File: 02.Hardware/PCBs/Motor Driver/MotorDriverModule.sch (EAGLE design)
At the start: 45 parts, among them Q1 DMC3021LSD-13, Q2 DMC3021LSD-13, Q3 DMC3021LSD-13, U1 FAN3268TMX, U2 FAN3268TMX, U3 FAN3268TMX, U4 MCP6001T-I_LT

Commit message: Minor modifications
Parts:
- added C9: (no value), rcl:C-EUC0805
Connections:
- net GND: now also C9.2
- net VCC: now also C9.1
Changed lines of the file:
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@@
 <part name="GND25" library="SparkFun-PowerSymbols" library_urn="urn:adsk.eagle:library:530" deviceset="GND" device=""/>
 <part name="J5" library="SparkFun-Connectors" library_urn="urn:adsk.eagle:library:513" deviceset="CONN_10" device="&quot;" package3d_urn="urn:adsk.eagle:package:38157/1"/>
+<part name="C9" library="rcl" library_urn="urn:adsk.eagle:library:334" deviceset="C-EU" device="C0805" package3d_urn="urn:adsk.eagle:package:23617/2"/>
+<part name="SUPPLY7" library="SparkFun-PowerSymbols" library_urn="urn:adsk.eagle:library:530" deviceset="VCC" device=""/>
+<part name="GND24" library="SparkFun-PowerSymbols" library_urn="urn:adsk.eagle:library:530" deviceset="GND" device=""/>
 </parts>
 <sheets>
@@
 <attribute name="NAME" x="330.2" y="78.232" size="1.778" layer="95" font="vector" rot="R180"/>
 </instance>
+<instance part="C9" gate="G$1" x="274.32" y="129.54" smashed="yes">
+<attribute name="NAME" x="275.844" y="129.921" size="1.778" layer="95"/>
+<attribute name="VALUE" x="275.844" y="124.841" size="1.778" layer="96"/>
+</instance>
+<instance part="SUPPLY7" gate="G$1" x="274.32" y="132.08" smashed="yes">
+<attribute name="VALUE" x="274.32" y="134.874" size="1.778" layer="96" align="bottom-center"/>
+</instance>
+<instance part="GND24" gate="1" x="274.32" y="121.92" smashed="yes">
+<attribute name="VALUE" x="274.32" y="121.666" size="1.778" layer="96" align="top-center"/>
+</instance>
 </instances>
 <busses>
@@
 <wire x1="320.04" y1="35.56" x2="302.26" y2="35.56" width="0.1524" layer="91"/>
 <label x="304.8" y="35.56" size="1.778" layer="95"/>
+</segment>
+<segment>
+<pinref part="C9" gate="G$1" pin="2"/>
+<pinref part="GND24" gate="1" pin="GND"/>
 </segment>
 </net>
@@
 <label x="304.8" y="33.02" size="1.778" layer="95"/>
 </segment>
-</net>
+<segment>
+<pinref part="C9" gate="G$1" pin="1"/>
+<pinref part="SUPPLY7" gate="G$1" pin="VCC"/>
+</segment>
+</net>

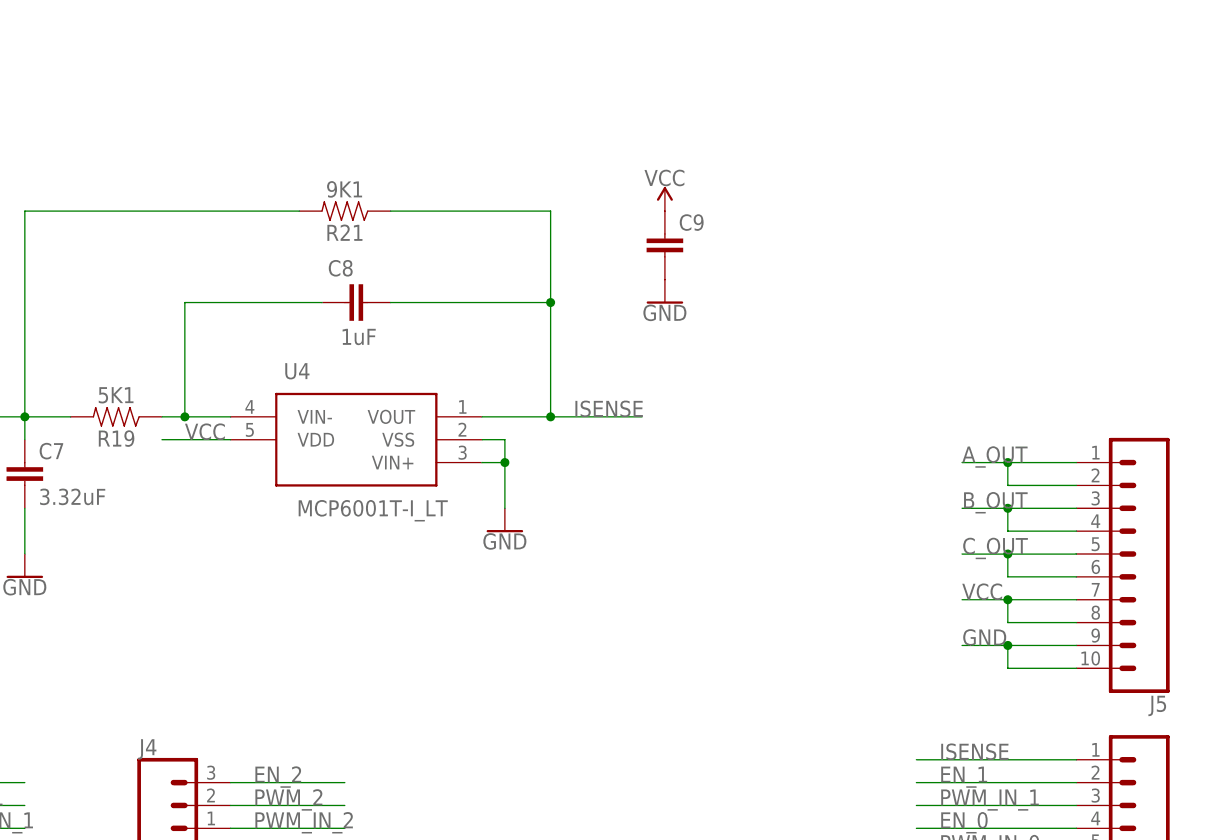
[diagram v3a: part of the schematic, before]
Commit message: añadido 3v3 a driver de motor
Para que el AO filtro de ISENSE se alimente a 3v3
Se actualiza GERBER para PCBWAY
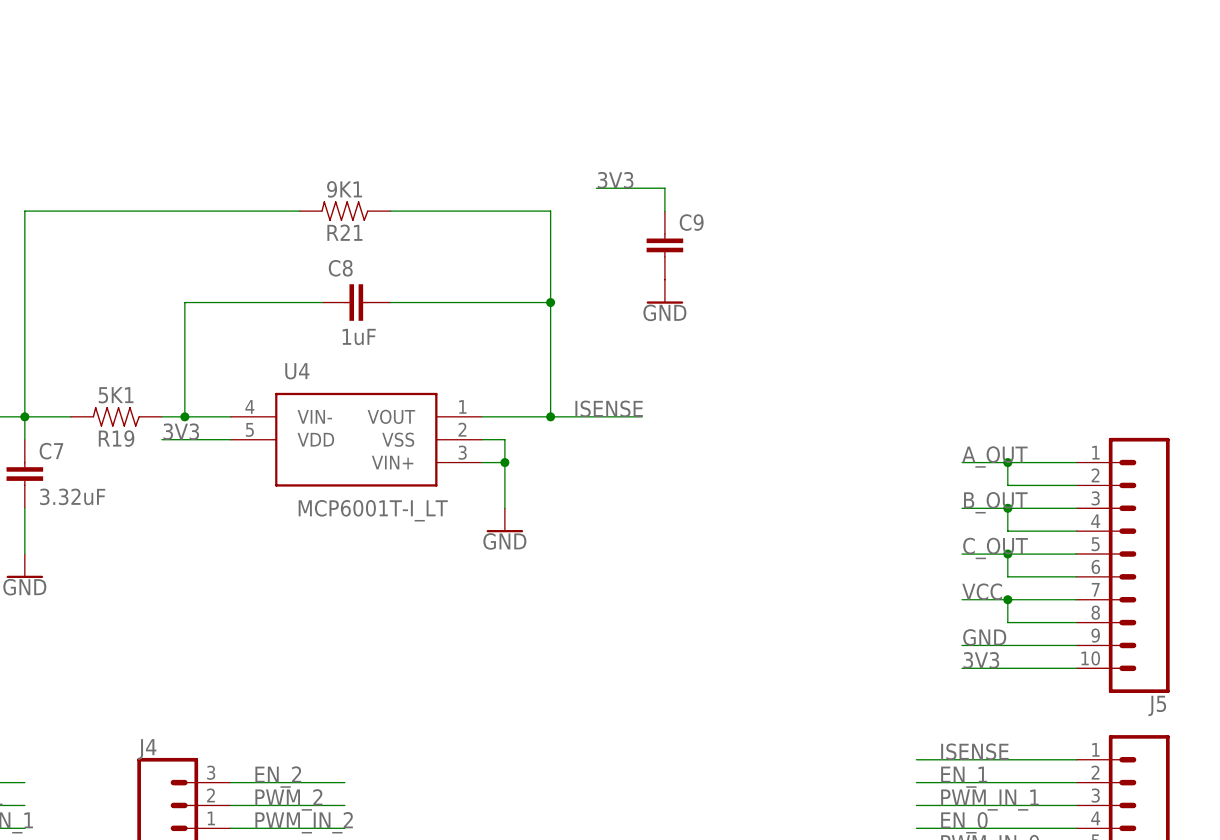
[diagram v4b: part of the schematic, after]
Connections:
- new net 3V3: C9.1, J5.10, U4.VDD
- net GND: no longer J5.10
- net VCC: no longer C9.1, U4.VDD
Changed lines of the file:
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@@
 <part name="J5" library="SparkFun-Connectors" library_urn="urn:adsk.eagle:library:513" deviceset="CONN_10" device="&quot;" package3d_urn="urn:adsk.eagle:package:38157/1"/>
 <part name="C9" library="rcl" library_urn="urn:adsk.eagle:library:334" deviceset="C-EU" device="C0805" package3d_urn="urn:adsk.eagle:package:23617/2"/>
-<part name="SUPPLY7" library="SparkFun-PowerSymbols" library_urn="urn:adsk.eagle:library:530" deviceset="VCC" device=""/>
 <part name="GND24" library="SparkFun-PowerSymbols" library_urn="urn:adsk.eagle:library:530" deviceset="GND" device=""/>
 </parts>
@@
 <attribute name="VALUE" x="275.844" y="124.841" size="1.778" layer="96"/>
 </instance>
-<instance part="SUPPLY7" gate="G$1" x="274.32" y="132.08" smashed="yes">
-<attribute name="VALUE" x="274.32" y="134.874" size="1.778" layer="96" align="bottom-center"/>
-</instance>
 <instance part="GND24" gate="1" x="274.32" y="121.92" smashed="yes">
 <attribute name="VALUE" x="274.32" y="121.666" size="1.778" layer="96" align="top-center"/>
@@
 <segment>
 <pinref part="J5" gate="G$1" pin="9"/>
-<wire x1="320.04" y1="83.82" x2="312.42" y2="83.82" width="0.1524" layer="91"/>
-<pinref part="J5" gate="G$1" pin="10"/>
-<wire x1="312.42" y1="83.82" x2="307.34" y2="83.82" width="0.1524" layer="91"/>
-<wire x1="320.04" y1="81.28" x2="312.42" y2="81.28" width="0.1524" layer="91"/>
-<wire x1="312.42" y1="81.28" x2="312.42" y2="83.82" width="0.1524" layer="91"/>
-<junction x="312.42" y="83.82"/>
+<wire x1="320.04" y1="83.82" x2="307.34" y2="83.82" width="0.1524" layer="91"/>
 <label x="307.34" y="83.82" size="1.778" layer="95"/>
 </segment>
@@
 </segment>
 <segment>
-<pinref part="U4" gate="G$1" pin="VDD"/>
-<wire x1="226.06" y1="106.68" x2="218.44" y2="106.68" width="0.1524" layer="91"/>
-<label x="220.98" y="106.68" size="1.778" layer="95"/>
-</segment>
-<segment>
 <pinref part="J5" gate="G$1" pin="7"/>
 <wire x1="320.04" y1="88.9" x2="312.42" y2="88.9" width="0.1524" layer="91"/>
@@
 <wire x1="320.04" y1="33.02" x2="302.26" y2="33.02" width="0.1524" layer="91"/>
 <label x="304.8" y="33.02" size="1.778" layer="95"/>
-</segment>
-<segment>
-<pinref part="C9" gate="G$1" pin="1"/>
-<pinref part="SUPPLY7" gate="G$1" pin="VCC"/>
 </segment>
 </net>
@@
 </segment>
 </net>
+<net name="3V3" class="0">
+<segment>
+<pinref part="J5" gate="G$1" pin="10"/>
+<wire x1="320.04" y1="81.28" x2="307.34" y2="81.28" width="0.1524" layer="91"/>
+<label x="307.34" y="81.28" size="1.778" layer="95"/>
+</segment>
+<segment>
+<pinref part="U4" gate="G$1" pin="VDD"/>
+<wire x1="226.06" y1="106.68" x2="218.44" y2="106.68" width="0.1524" layer="91"/>
+<label x="218.44" y="106.68" size="1.778" layer="95"/>
+</segment>
+<segment>
+<pinref part="C9" gate="G$1" pin="1"/>
+<wire x1="274.32" y1="132.08" x2="274.32" y2="134.62" width="0.1524" layer="91"/>
+<wire x1="274.32" y1="134.62" x2="266.7" y2="134.62" width="0.1524" layer="91"/>
+<label x="266.7" y="134.62" size="1.778" layer="95"/>
+</segment>
+</net>

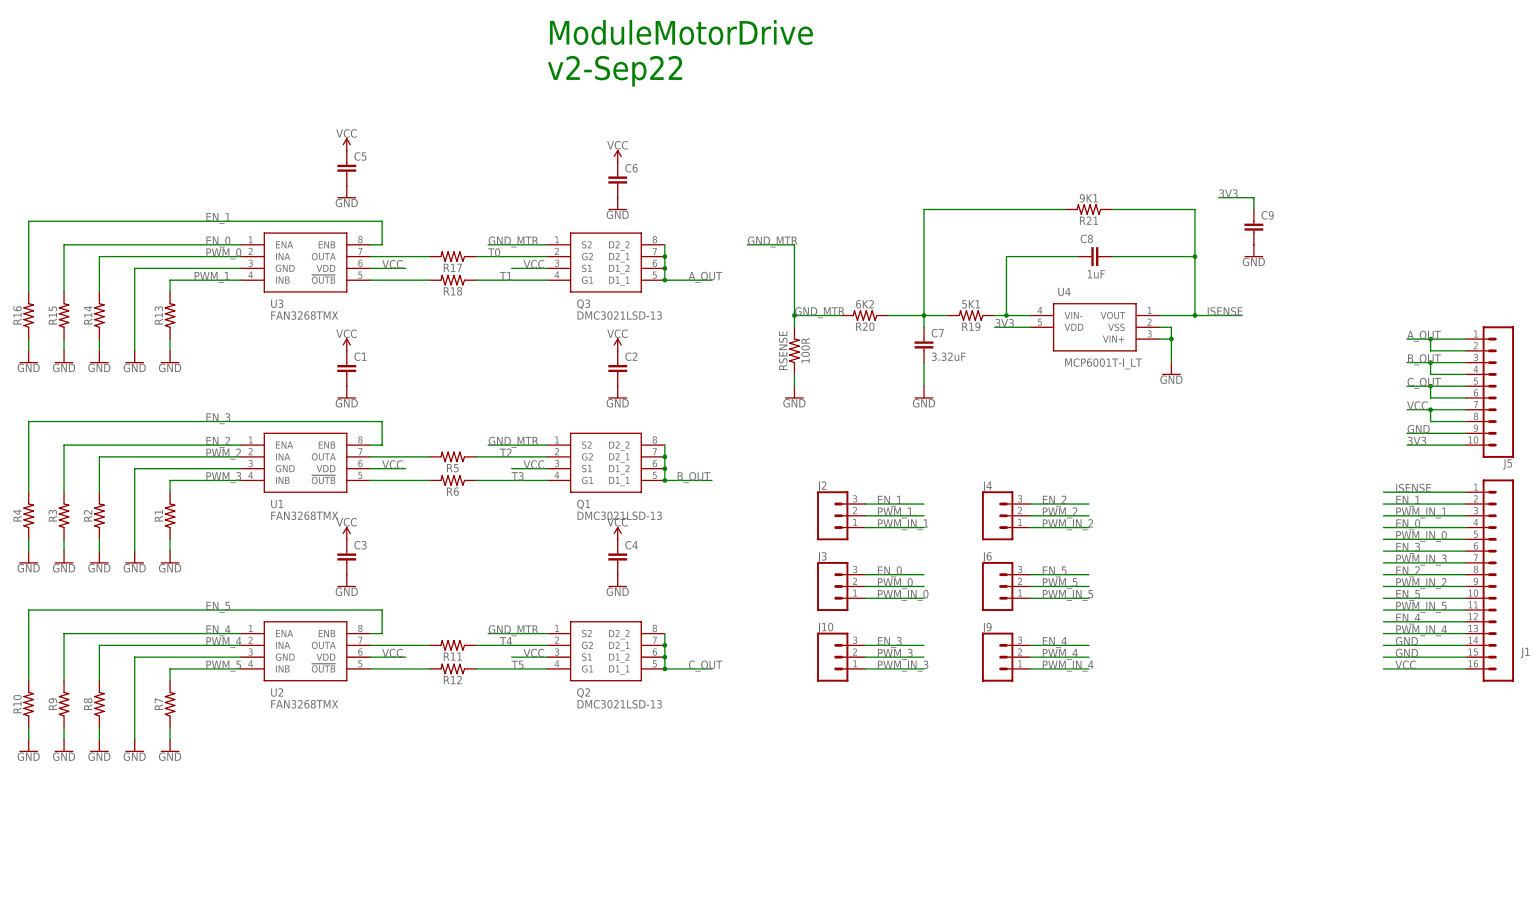
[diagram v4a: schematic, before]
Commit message: Se mueve resistencia de pull-down entrada a pull-down en MOSFET
Para conseguir crear un tDEAD entre transistores
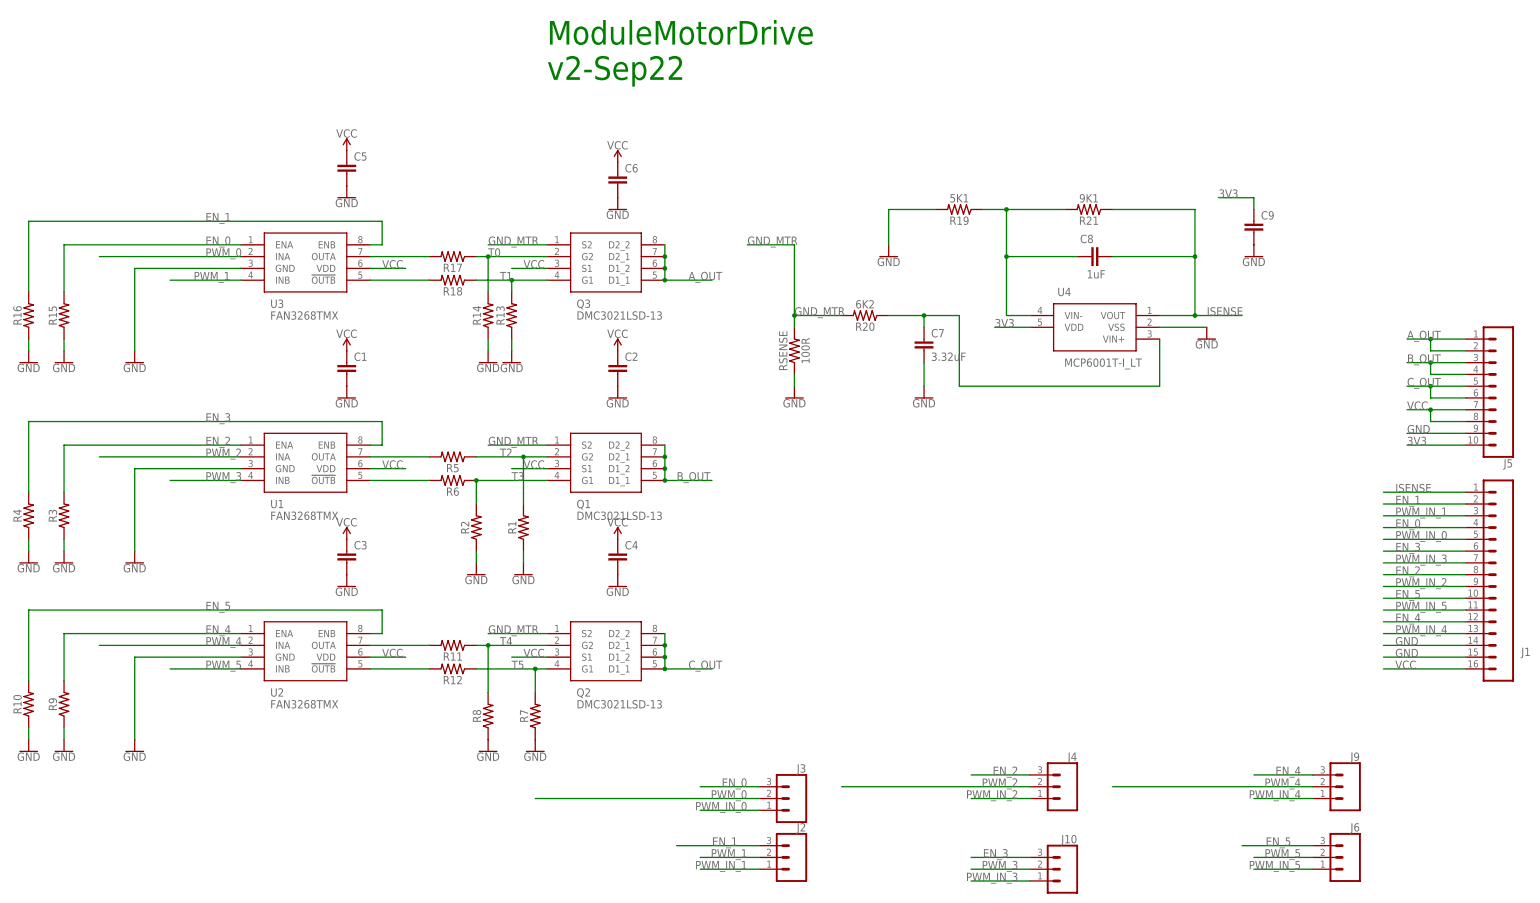
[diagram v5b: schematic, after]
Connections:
- removed net N$1: C7.1, R19.2, R20.1, R21.2
- new net N$3: C7.1, R20.1, U4.VIN+
- net GND: now also R19.2; no longer U4.VIN+
- net N$2: now also R21.2
- net PWM_0: no longer R14.2
- net PWM_1: no longer R13.2
- net PWM_2: no longer R2.2
- net PWM_3: no longer R1.2
- net PWM_4: no longer R8.2
- net PWM_5: no longer R7.2
- net T0: now also R14.2
- net T1: now also R13.2
- net T2: now also R1.2
- net T3: now also R2.2
- net T4: now also R8.2
- net T5: now also R7.2
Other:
- moved on the sheet: J10, J2, J3, J4, J6, J9, R1, R13, R14, R19, R2, R7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
